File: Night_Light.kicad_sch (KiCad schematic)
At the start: 10 parts, among them J1 3V0, Q1 2N3904

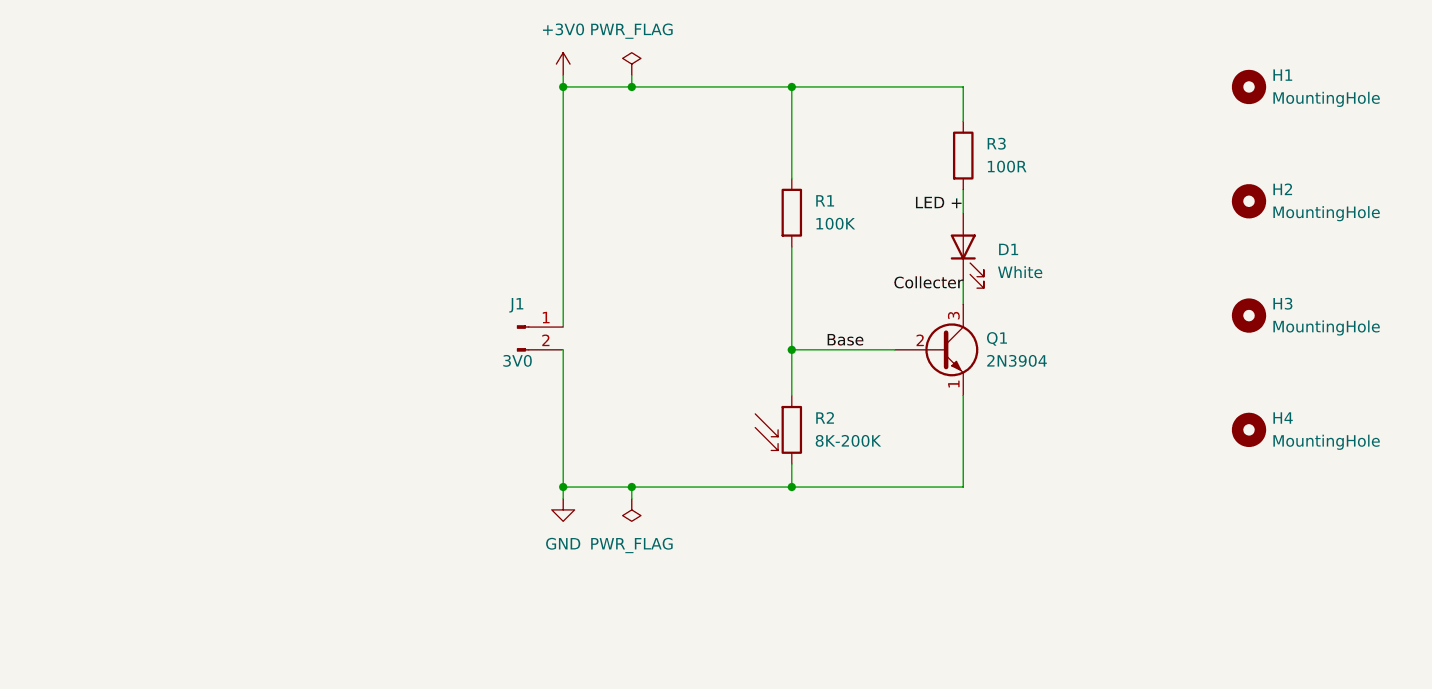
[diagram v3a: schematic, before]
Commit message: Remove mounting holes. Reduce size to 1.0x1.0. Changed some footprints to match real board.
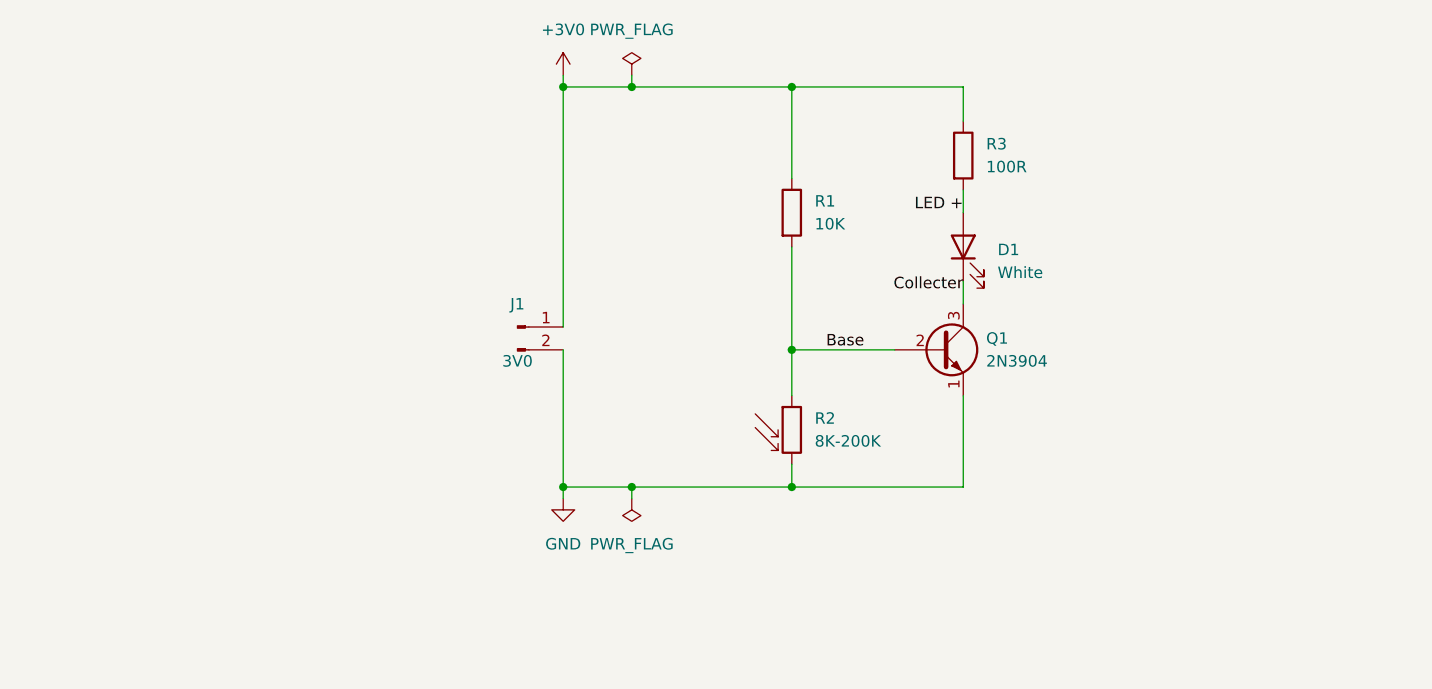
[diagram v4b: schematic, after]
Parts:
- removed H1, H2, H3, H4: MountingHole, MountingHole:MountingHole_3.2mm_M3, symbol Mechanical:MountingHole
- Q1: footprint Package_TO_SOT_THT:TO-92_HandSolder -> Package_TO_SOT_THT:TO-92_Inline_Wide
- R1: value 100K -> 10K
- R2: footprint OptoDevice:R_LDR_4.9x4.2mm_P2.54mm_Vertical -> OptoDevice:R_LDR_7x6mm_P5.1mm_Vertical
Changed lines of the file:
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@@
     (effects (font (size 1.27 1.27)) (justify right bottom))
-  )
-  (symbol (lib_id "Mechanical:MountingHole") (at 190.5 88.9 0) (unit 1)
-    (in_bom yes) (on_board yes) (fields_autoplaced)
-    (property "Reference" "H2" (id 0) (at 193.04 87.6299 0)
-      (effects (font (size 1.27 1.27)) (justify left))
-    )
-    (property "Value" "MountingHole" (id 1) (at 193.04 90.1699 0)
-      (effects (font (size 1.27 1.27)) (justify left))
-    )
-    (property "Footprint" "MountingHole:MountingHole_3.2mm_M3" (id 2) (at 190.5 88.9 0)
-      (effects (font (size 1.27 1.27)) hide)
-    )
-    (property "Datasheet" "~" (id 3) (at 190.5 88.9 0)
-      (effects (font (size 1.27 1.27)) hide)
-    )
   )
   (symbol (lib_id "power:PWR_FLAG") (at 121.92 121.92 180) (unit 1)
@@
       (effects (font (size 1.27 1.27)) (justify left))
     )
-    (property "Footprint" "OptoDevice:R_LDR_4.9x4.2mm_P2.54mm_Vertical" (id 2) (at 140.97 120.65 90)
+    (property "Footprint" "OptoDevice:R_LDR_7x6mm_P5.1mm_Vertical" (id 2) (at 140.97 120.65 90)
       (effects (font (size 1.27 1.27)) (justify left) hide)
     )
@@
       (effects (font (size 1.27 1.27)) (justify left))
     )
-    (property "Footprint" "Package_TO_SOT_THT:TO-92_HandSolder" (id 2) (at 161.29 102.87 0)
+    (property "Footprint" "Package_TO_SOT_THT:TO-92_Inline_Wide" (id 2) (at 161.29 102.87 0)
       (effects (font (size 1.27 1.27)) hide)
     )
@@
     (pin "2")
     (pin "3")
-  )
-  (symbol (lib_id "Mechanical:MountingHole") (at 190.5 101.6 0) (unit 1)
-    (in_bom yes) (on_board yes) (fields_autoplaced)
-    (property "Reference" "H3" (id 0) (at 193.04 100.3299 0)
-      (effects (font (size 1.27 1.27)) (justify left))
-    )
-    (property "Value" "MountingHole" (id 1) (at 193.04 102.8699 0)
-      (effects (font (size 1.27 1.27)) (justify left))
-    )
-    (property "Footprint" "MountingHole:MountingHole_3.2mm_M3" (id 2) (at 190.5 101.6 0)
-      (effects (font (size 1.27 1.27)) hide)
-    )
-    (property "Datasheet" "~" (id 3) (at 190.5 101.6 0)
-      (effects (font (size 1.27 1.27)) hide)
-    )
   )
   (symbol (lib_id "power:PWR_FLAG") (at 121.92 74.93 0) (unit 1)
@@
       (effects (font (size 1.27 1.27)) (justify left))
     )
-    (property "Value" "100K" (id 1) (at 142.24 91.4399 0)
+    (property "Value" "10K" (id 1) (at 142.24 91.4399 0)
       (effects (font (size 1.27 1.27)) (justify left))
     )
@@
     (pin "1")
     (pin "2")
-  )
-  (symbol (lib_id "Mechanical:MountingHole") (at 190.5 76.2 0) (unit 1)
-    (in_bom yes) (on_board yes) (fields_autoplaced)
-    (property "Reference" "H1" (id 0) (at 193.04 74.9299 0)
-      (effects (font (size 1.27 1.27)) (justify left))
-    )
-    (property "Value" "MountingHole" (id 1) (at 193.04 77.4699 0)
-      (effects (font (size 1.27 1.27)) (justify left))
-    )
-    (property "Footprint" "MountingHole:MountingHole_3.2mm_M3" (id 2) (at 190.5 76.2 0)
-      (effects (font (size 1.27 1.27)) hide)
-    )
-    (property "Datasheet" "~" (id 3) (at 190.5 76.2 0)
-      (effects (font (size 1.27 1.27)) hide)
-    )
   )
   (symbol (lib_id "power:GND") (at 114.3 121.92 0) (unit 1)
@@
     (pin "2")
   )
-  (symbol (lib_id "Mechanical:MountingHole") (at 190.5 114.3 0) (unit 1)
-    (in_bom yes) (on_board yes) (fields_autoplaced)
-    (property "Reference" "H4" (id 0) (at 193.04 113.0299 0)
-      (effects (font (size 1.27 1.27)) (justify left))
-    )
-    (property "Value" "MountingHole" (id 1) (at 193.04 115.5699 0)
-      (effects (font (size 1.27 1.27)) (justify left))
-    )
-    (property "Footprint" "MountingHole:MountingHole_3.2mm_M3" (id 2) (at 190.5 114.3 0)
-      (effects (font (size 1.27 1.27)) hide)
-    )
-    (property "Datasheet" "~" (id 3) (at 190.5 114.3 0)
-      (effects (font (size 1.27 1.27)) hide)
-    )
-  )
   (sheet_instances
     (path "/" (page "1"))
@@
       (reference "D1") (unit 1) (value "White") (footprint "LED_THT:LED_D5.0mm_Clear")
     )
-    (path "/b94e18e5-229f-42d2-884f-7340cf4b6b2f"
-      (reference "H1") (unit 1) (value "MountingHole") (footprint "MountingHole:MountingHole_3.2mm_M3")
-    )
-    (path "/0ac740bb-41de-498f-b8cf-44b95da6496c"
-      (reference "H2") (unit 1) (value "MountingHole") (footprint "MountingHole:MountingHole_3.2mm_M3")
-    )
-    (path "/3ed663e4-8115-46bd-8d89-7a1ef10cd914"
-      (reference "H3") (unit 1) (value "MountingHole") (footprint "MountingHole:MountingHole_3.2mm_M3")
-    )
-    (path "/fb23aa04-ed5e-400a-b61e-5eb0cfde2b1a"
-      (reference "H4") (unit 1) (value "MountingHole") (footprint "MountingHole:MountingHole_3.2mm_M3")
-    )
     (path "/47e2e0a1-3a67-409e-ac27-e47ce2e08aac"
       (reference "J1") (unit 1) (value "3V0") (footprint "Connector_Wire:SolderWire-1.5sqmm_1x02_P6mm_D1.7mm_OD3mm")
     )
     (path "/21529b31-fbed-4aa1-8161-987b99b8bb72"
-      (reference "Q1") (unit 1) (value "2N3904") (footprint "Package_TO_SOT_THT:TO-92_HandSolder")
+      (reference "Q1") (unit 1) (value "2N3904") (footprint "Package_TO_SOT_THT:TO-92_Inline_Wide")
     )
     (path "/88e923cf-fa2e-4fa3-9130-af5a72349912"
-      (reference "R1") (unit 1) (value "100K") (footprint "Resistor_THT:R_Axial_DIN0207_L6.3mm_D2.5mm_P10.16mm_Horizontal")
+      (reference "R1") (unit 1) (value "10K") (footprint "Resistor_THT:R_Axial_DIN0207_L6.3mm_D2.5mm_P10.16mm_Horizontal")
     )
     (path "/18d72c6c-48f1-4f58-b4bd-603b0d4cbbcb"
-      (reference "R2") (unit 1) (value "8K-200K") (footprint "OptoDevice:R_LDR_4.9x4.2mm_P2.54mm_Vertical")
+      (reference "R2") (unit 1) (value "8K-200K") (footprint "OptoDevice:R_LDR_7x6mm_P5.1mm_Vertical")
     )
     (path "/efe1dff2-774b-43d6-b07c-abd5c4f91b66"

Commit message: Updated silkscreen and version
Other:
- company: Zach Dribin -> Julian Jayhawks
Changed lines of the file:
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@@
   (title_block
     (title "Night Light")
-    (date "2023-01-05")
-    (company "Zach Dribin")
+    (date "2023-02-04")
+    (rev "1.0.0")
+    (company "Julian Jayhawks")
+    (comment 1 "Zach Dribin")
   )
   (junction (at 121.92 76.2) (diameter 0) (color 0 0 0 0)
